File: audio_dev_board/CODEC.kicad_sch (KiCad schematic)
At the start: 17 parts, among them IC1 CS4270-CZZR

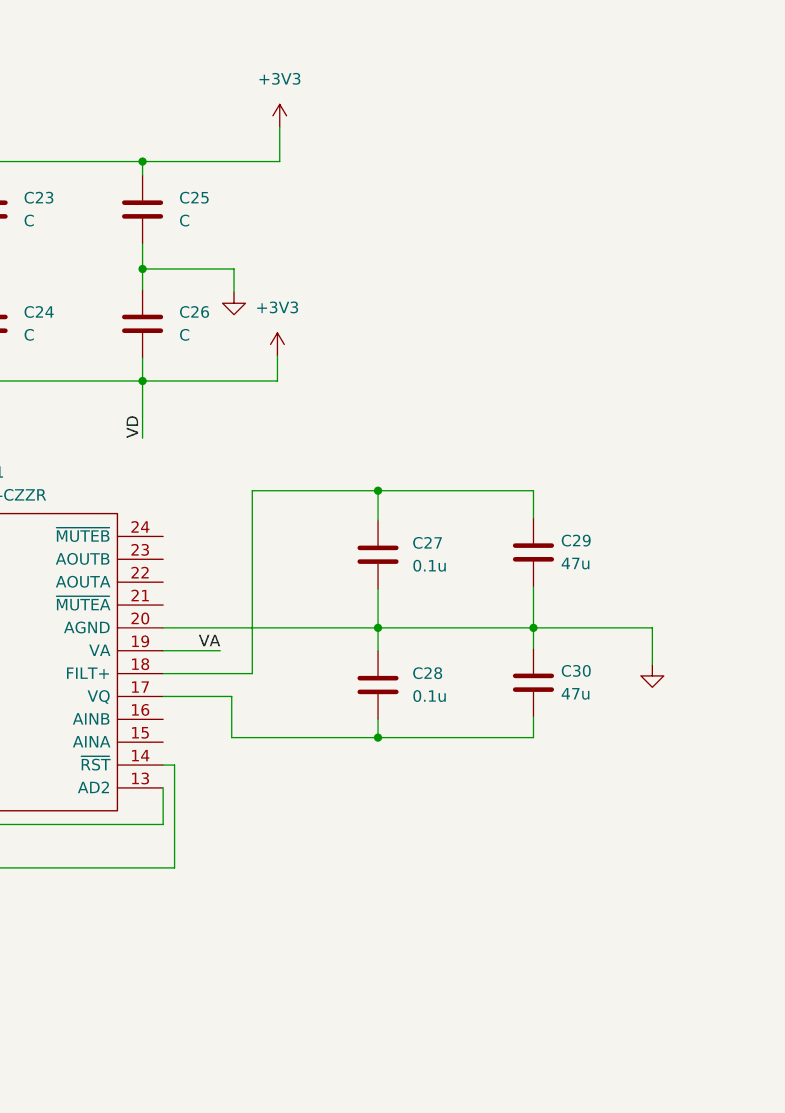
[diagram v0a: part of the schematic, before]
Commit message: added more scems
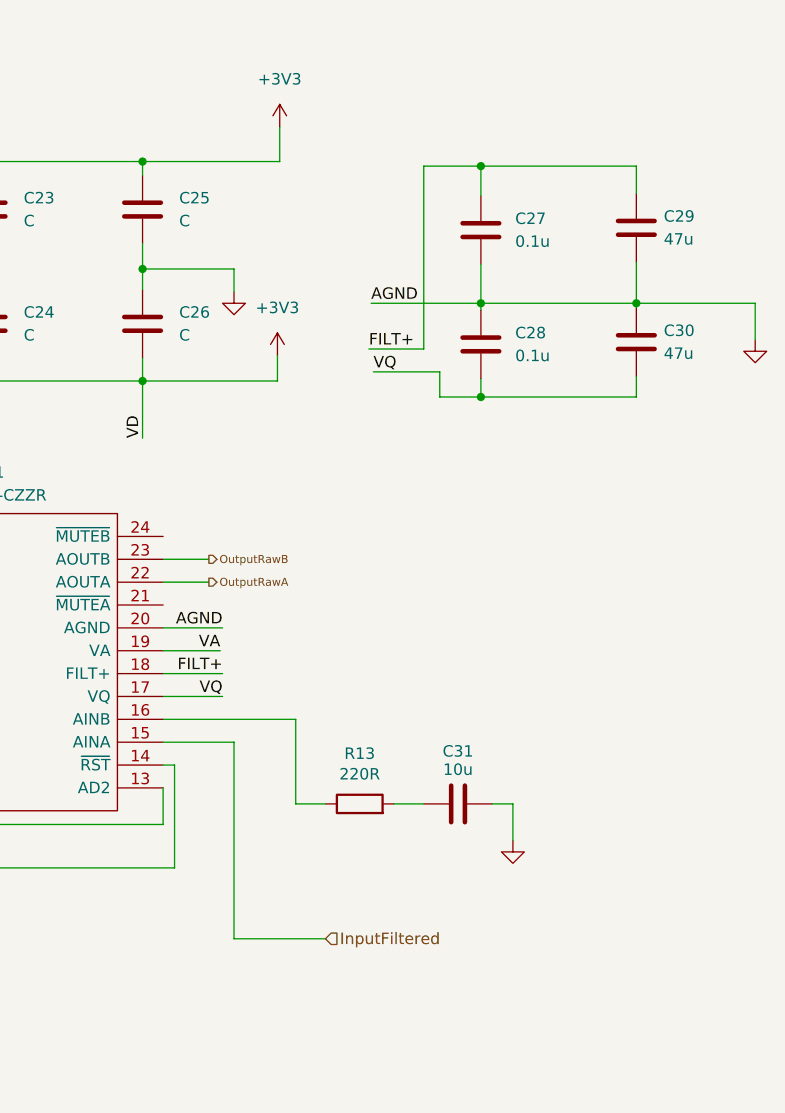
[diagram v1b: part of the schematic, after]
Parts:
- added C31: 10u, symbol Device:C
- added R13: 220R, symbol Device:R
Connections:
- net GND: now also C31.2
- net VQ: now reaches C28.2, C30.2, IC1.17 (VQ)
- net FILT+: now reaches C27.1, C29.1, IC1.18 (FILT+)
- net InputFiltered: now reaches IC1.15 (AINA)
- net at IC1.16 (AINB): now also R13.1
- net OutputRawA: now reaches IC1.22 (AOUTA)
- net OutputRawB: now reaches IC1.23 (AOUTB)
- new net: C31.1, R13.2
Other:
- moved on the sheet: C27, C28, C29, C30

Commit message: bluhhh
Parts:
- removed C31: 10u, symbol Device:C
- removed R13: 220R, symbol Device:R
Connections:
- net InputBFiltered: now reaches IC1.16 (AINB)
- net InputFiltered renamed InputAFiltered
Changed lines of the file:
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@@
-	(wire
-		(pts
-			(xy 268.224 151.13) (xy 268.224 155.194)
-		)
-		(stroke
-			(width 0)
-			(type default)
-		)
-	)
 	(wire
 		(pts
@@
 	(wire
 		(pts
-			(xy 255.016 151.13) (xy 258.318 151.13)
-		)
-		(stroke
-			(width 0)
-			(type default)
-		)
-	)
-	(wire
-		(pts
 			(xy 182.626 177.292) (xy 191.262 177.292)
 		)
@@
 	(wire
 		(pts
-			(xy 265.938 151.13) (xy 268.224 151.13)
-		)
-		(stroke
-			(width 0)
-			(type default)
-		)
-	)
-	(wire
-		(pts
 			(xy 252.222 100.584) (xy 258.318 100.584)
 		)
@@
 			(width 0)
 			(type default)
+		)
+	)
+	(rectangle
+		(start 117.856 66.548)
+		(end 307.594 192.786)
+		(stroke
+			(width 0.75)
+			(type default)
+		)
+		(fill
+			(type none)
 		)
 	)
 	(text "Codec"
 		(exclude_from_sim no)
-		(at 43.434 30.988 0)
+		(at 136.652 57.658 0)
 		(effects
 			(font
@@
 		)
 	)
+	(hierarchical_label "InputBFiltered"
+		(shape input)
+		(at 247.396 151.13 0)
+		(effects
+			(font
+				(size 1.27 1.27)
+			)
+			(justify left)
+		)
+	)
 	(hierarchical_label "OutputRawA"
 		(shape output)
@@
 		)
 	)
-	(hierarchical_label "InputFiltered"
+	(hierarchical_label "InputAFiltered"
 		(shape input)
 		(at 247.396 166.116 0)
@@
 	)
 	(symbol
-		(lib_id "Device:C")
-		(at 262.128 151.13 90)
-		(unit 1)
-		(exclude_from_sim no)
-		(in_bom yes)
-		(on_board yes)
-		(dnp no)
-		(property "Reference" "C31"
-			(at 262.128 145.288 90)
-			(effects
-				(font
-					(size 1.27 1.27)
-				)
-			)
-		)
-		(property "Value" "10u"
-			(at 262.128 147.32 90)
-			(effects
-				(font
-					(size 1.27 1.27)
-				)
-			)
-		)
-		(property "Footprint" ""
-			(at 265.938 150.1648 0)
-			(effects
-				(font
-					(size 1.27 1.27)
-				)
-				(hide yes)
-			)
-		)
-		(property "Datasheet" "~"
-			(at 262.128 151.13 0)
-			(effects
-				(font
-					(size 1.27 1.27)
-				)
-				(hide yes)
-			)
-		)
-		(property "Description" "Unpolarized capacitor"
-			(at 262.128 151.13 0)
-			(effects
-				(font
-					(size 1.27 1.27)
-				)
-				(hide yes)
-			)
-		)
-		(pin "1"
-		)
-		(pin "2"
-		)
-		(instances
-			(project ""
-				(path "/9f0c82f0-eba2-4eef-9ea0-d089929edc65/b47d1b7e-a98d-4201-91ae-d062d458d2a3"
-					(reference "C31")
-					(unit 1)
-				)
-			)
-		)
-	)
-	(symbol
 		(lib_id "Device:R")
 		(at 167.64 167.386 0)
@@
 	)
 	(symbol
-		(lib_id "Device:R")
-		(at 251.206 151.13 90)
-		(unit 1)
-		(exclude_from_sim no)
-		(in_bom yes)
-		(on_board yes)
-		(dnp no)
-		(property "Reference" "R13"
-			(at 251.206 145.542 90)
-			(effects
-				(font
-					(size 1.27 1.27)
-				)
-			)
-		)
-		(property "Value" "220R"
-			(at 251.206 147.828 90)
-			(effects
-				(font
-					(size 1.27 1.27)
-				)
-			)
-		)
-		(property "Footprint" ""
-			(at 251.206 152.908 90)
-			(effects
-				(font
-					(size 1.27 1.27)
-				)
-				(hide yes)
-			)
-		)
-		(property "Datasheet" "~"
-			(at 251.206 151.13 0)
-			(effects
-				(font
-					(size 1.27 1.27)
-				)
-				(hide yes)
-			)
-		)
-		(property "Description" "Resistor"
-			(at 251.206 151.13 0)
-			(effects
-				(font
-					(size 1.27 1.27)
-				)
-				(hide yes)
-			)
-		)
-		(pin "2"
-		)
-		(pin "1"
-		)
-		(instances
-			(project ""
-				(path "/9f0c82f0-eba2-4eef-9ea0-d089929edc65/b47d1b7e-a98d-4201-91ae-d062d458d2a3"
-					(reference "R13")
-					(unit 1)
-				)
-			)
-		)
-	)
-	(symbol
 		(lib_id "power:+3V3")
 		(at 242.062 101.346 0)
@@
 					(unit 1)
 				)
-			)
-		)
-	)
-	(symbol
-		(lib_id "power:GND")
-		(at 268.224 155.194 0)
-		(unit 1)
-		(exclude_from_sim no)
-		(in_bom yes)
-		(on_board yes)
-		(dnp no)
-		(fields_autoplaced yes)
-		(property "Reference" "#PWR033"
-			(at 268.224 161.544 0)
-			(effects
-				(font
-					(size 1.27 1.27)
-				)
-				(hide yes)
-			)
-		)
-		(property "Value" "GND"
-			(at 268.224 160.528 0)
-			(effects
-				(font
-					(size 1.27 1.27)
-				)
-				(hide yes)
-			)
-		)
-		(property "Footprint" ""
-			(at 268.224 155.194 0)
-			(effects
-				(font
-					(size 1.27 1.27)
-				)
-				(hide yes)
-			)
-		)
-		(property "Datasheet" ""
-			(at 268.224 155.194 0)
-			(effects
-				(font
-					(size 1.27 1.27)
-				)
-				(hide yes)
-			)
-		)
-		(property "Description" "Power symbol creates a global label with name \"GND\" , ground"
-			(at 268.224 155.194 0)
-			(effects
-				(font
-					(size 1.27 1.27)
-				)
-				(hide yes)
-			)
-		)
-		(pin "1"
-		)
-		(instances
-			(project ""
-				(path "/9f0c82f0-eba2-4eef-9ea0-d089929edc65/b47d1b7e-a98d-4201-91ae-d062d458d2a3"
-					(reference "#PWR033")
-					(unit 1)
-				)
